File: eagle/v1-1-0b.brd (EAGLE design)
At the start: 313 x 132.9 mm, 176 parts, among them J1 CR22A-44D-2.54DSA(70), J3 26-60-4040, J4 AUDIO_JACK_3.5MM_PTH, J5 DIN5, SW1 3PDT-AQ-SWITCH, SW2 9077-1, U10 7805, U11 74LS10N, U13 74LS04N, U14 4528N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

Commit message: 8/19/2020 updates
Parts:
- removed JP4: (no value), aquarius2:1X01
- added JP1: (no value), aquarius2:1X01
- moved JP2 5.93 mm to (144.5, 48.1)
- moved JP3 4.06 mm to (148.6, 48.0)
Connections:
- net N$122: now also JP1.1; no longer JP2.1
- net N$19: now also JP2.1; no longer JP3.1
- net PALSW: now also JP3.1; no longer JP4.1
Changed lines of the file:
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@@
 <layer number="47" name="Measures" color="7" fill="1" visible="yes" active="yes"/>
 <layer number="48" name="Document" color="7" fill="1" visible="no" active="yes"/>
-<layer number="49" name="Reference" color="7" fill="1" visible="no" active="yes"/>
+<layer number="49" name="Reference" color="7" fill="1" visible="yes" active="yes"/>
 <layer number="50" name="dxf" color="7" fill="1" visible="yes" active="yes"/>
 <layer number="51" name="tDocu" color="7" fill="1" visible="yes" active="yes"/>
@@
 <wire x1="44.45" y1="9.906" x2="45.974" y2="11.6078" width="0.0762" layer="21"/>
 <wire x1="45.974" y1="11.6078" x2="45.974" y2="11.176" width="0.0762" layer="21"/>
+<frame x1="-11.176" y1="-13.462" x2="333.248" y2="144.78" columns="5" rows="3" layer="49"/>
 </plain>
 <attributes>
@@
 <attribute name="NAME" x="144.2974" y="30.3784" size="1.27" layer="21"/>
 </element>
-<element name="JP2" library="aquarius2" package="1X01" package3d_urn="urn:adsk.eagle:package:22485/2" value="" x="148.5392" y="43.7134" smashed="yes">
+<element name="JP1" library="aquarius2" package="1X01" package3d_urn="urn:adsk.eagle:package:22485/2" value="" x="148.5392" y="43.7134" smashed="yes">
 <attribute name="POPULARITY" value="64" x="148.5392" y="43.7134" size="1.778" layer="27" display="off"/>
 <attribute name="VALUE" x="147.2692" y="40.5384" size="1.27" layer="27"/>
 </element>
-<element name="JP3" library="aquarius2" package="1X01" package3d_urn="urn:adsk.eagle:package:22485/2" value="" x="144.5006" y="48.0568" smashed="yes">
+<element name="JP2" library="aquarius2" package="1X01" package3d_urn="urn:adsk.eagle:package:22485/2" value="" x="144.5006" y="48.0568" smashed="yes">
 <attribute name="POPULARITY" value="64" x="144.5006" y="48.0568" size="1.778" layer="27" display="off"/>
 <attribute name="VALUE" x="143.2306" y="44.8818" size="1.27" layer="27"/>
 </element>
-<element name="JP4" library="aquarius2" package="1X01" package3d_urn="urn:adsk.eagle:package:22485/2" value="" x="148.5646" y="48.0314" smashed="yes">
+<element name="JP3" library="aquarius2" package="1X01" package3d_urn="urn:adsk.eagle:package:22485/2" value="" x="148.5646" y="48.0314" smashed="yes">
 <attribute name="POPULARITY" value="64" x="148.5646" y="48.0314" size="1.778" layer="27" display="off"/>
 <attribute name="VALUE" x="147.2946" y="44.8564" size="1.27" layer="27"/>
@@
 </element>
 <element name="C22" library="aq-rcl" package="C050-025X085" value=".1uF" x="46.6852" y="45.9486" smashed="yes" rot="R270">
-<attribute name="NAME" x="46.6852" y="50.5206" size="0.8128" layer="25" ratio="10" align="bottom-center"/>
+<attribute name="NAME" x="46.6852" y="50.5206" size="0.6096" layer="25" ratio="10" align="bottom-center"/>
+<attribute name="VALUE" x="46.6852" y="41.3766" size="0.6096" layer="27" ratio="10" align="top-center"/>
 </element>
 <element name="C26" library="aq-rcl" package="C050-025X085" value=".1uF" x="11.8618" y="45.7962" smashed="yes" rot="R270">
@@
 </element>
 <element name="C20" library="aq-rcl" package="C050-025X090" value=".1uF" x="84.4296" y="45.2882" smashed="yes" rot="R270">
-<attribute name="NAME" x="84.4296" y="50.2412" size="0.8128" layer="25" ratio="10" align="bottom-center"/>
+<attribute name="NAME" x="84.4296" y="50.2412" size="0.6096" layer="25" ratio="10" align="bottom-center"/>
+<attribute name="VALUE" x="84.4296" y="40.4622" size="0.6096" layer="27" ratio="10" align="top-center"/>
 </element>
 <element name="C30" library="aq-rcl" package="E2,5-6" package3d_urn="urn:adsk.eagle:package:23349/1" value="10uF @ 16v" x="142.4686" y="60.579" smashed="yes" rot="R270">
@@
 </element>
 <element name="C36" library="aq-rcl" package="C050-024X044" package3d_urn="urn:adsk.eagle:package:23643/1" value=".01uF" x="137.9728" y="92.4306" smashed="yes">
-<attribute name="NAME" x="135.8138" y="93.8276" size="0.8128" layer="25" ratio="10"/>
+<attribute name="NAME" x="135.5598" y="93.8276" size="0.8128" layer="25" ratio="10"/>
 <attribute name="POPULARITY" value="14" x="137.9728" y="92.4306" size="1.778" layer="27" display="off"/>
 <attribute name="SPICEPREFIX" value="C" x="137.9728" y="92.4306" size="1.778" layer="27" display="off"/>
+<attribute name="VALUE" x="138.3538" y="93.8276" size="0.8128" layer="27" ratio="10"/>
 </element>
 <element name="C17" library="aq-rcl" package="C050-025X090" value=".1uF" x="81.661" y="68.453" smashed="yes" rot="R270">
@@
 <attribute name="POPULARITY" value="14" x="195.1736" y="81.2038" size="1.778" layer="27" display="off"/>
 <attribute name="SPICEPREFIX" value="C" x="195.1736" y="81.2038" size="1.778" layer="27" display="off"/>
+<attribute name="VALUE" x="195.7578" y="82.6262" size="0.8128" layer="27" ratio="10"/>
 </element>
 <element name="XTAL1" library="special" library_urn="urn:adsk.eagle:library:367" package="Q" package3d_urn="urn:adsk.eagle:package:26649/1" value="" x="177.673" y="88.9" smashed="yes" rot="R180">
@@
 <wire x1="115.70919375" y1="50.1904" x2="115.70919375" y2="46.67300625" width="0.508" layer="1"/>
 <wire x1="117.1194" y1="45.2628" x2="115.70919375" y2="46.67300625" width="0.508" layer="1"/>
-<contactref element="JP2" pad="1"/>
+<contactref element="JP1" pad="1"/>
 <wire x1="148.5392" y1="43.7134" x2="148.4884" y2="43.6626" width="0.508" layer="1"/>
 <wire x1="148.4884" y1="43.6626" x2="146.431" y2="43.6626" width="0.508" layer="1"/>
@@
 <wire x1="180.848" y1="81.026" x2="184.5564" y2="77.3176" width="0.508" layer="1"/>
 <wire x1="184.5564" y1="77.3176" x2="184.5564" y2="71.9582" width="0.508" layer="1"/>
-<contactref element="JP4" pad="1"/>
+<contactref element="JP3" pad="1"/>
 <wire x1="148.5646" y1="48.0314" x2="148.5392" y2="48.0568" width="0.508" layer="16"/>
 <wire x1="148.5392" y1="48.0568" x2="148.5392" y2="50.3936" width="0.508" layer="16"/>
@@
 <wire x1="140.4874" y1="50.1904" x2="140.4874" y2="49.0728" width="0.508" layer="1"/>
 <wire x1="141.9352" y1="47.625" x2="140.4874" y2="49.0728" width="0.508" layer="1"/>
-<contactref element="JP3" pad="1"/>
+<contactref element="JP2" pad="1"/>
 <wire x1="144.5006" y1="48.0568" x2="144.0688" y2="47.625" width="0.508" layer="1"/>
 <wire x1="144.0688" y1="47.625" x2="141.9352" y2="47.625" width="0.508" layer="1"/>

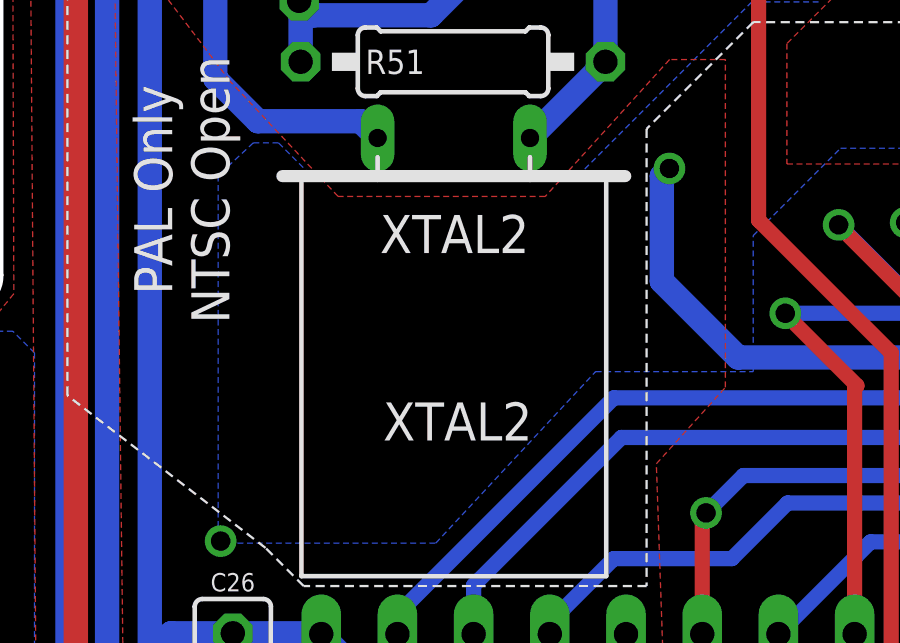
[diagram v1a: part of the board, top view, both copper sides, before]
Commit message: Edits for component values
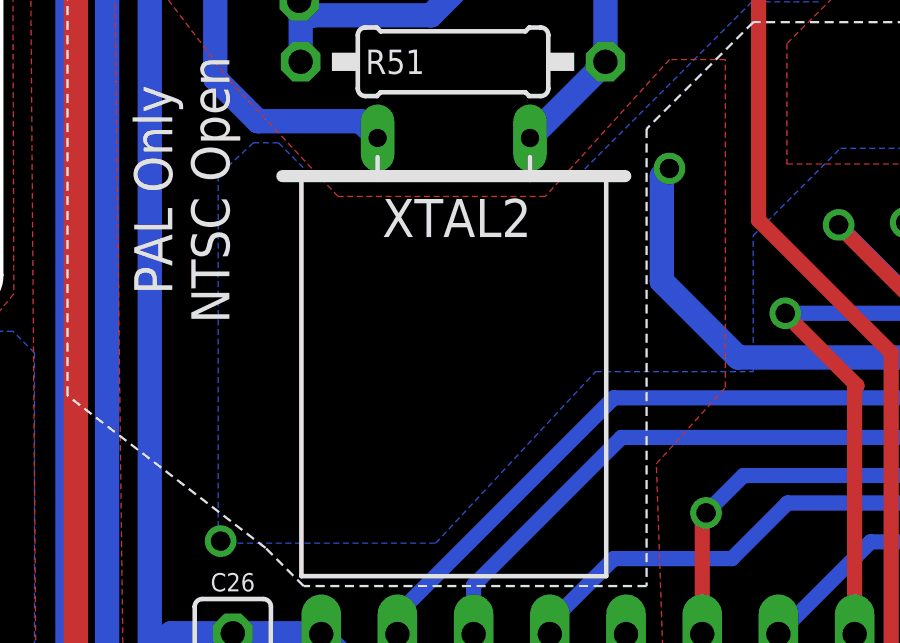
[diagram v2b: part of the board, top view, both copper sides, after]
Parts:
- XTAL1: value (none) -> 7.15909 MhZ
- XTAL2: value (none) -> 7.15909 Mhz
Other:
- board text added: "PAL 8.867238 Mhz"
- board text removed: "XTAL2"
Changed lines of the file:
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@@
 <text x="241.808" y="35.306" size="1.778" layer="21" align="center">Z80 CPU</text>
 <text x="108.966" y="114.3" size="1.778" layer="21" align="center">RF Modulator</text>
-<text x="19.2532" y="62.2808" size="1.27" layer="21" rot="R180" align="center">XTAL2</text>
 <text x="266.7" y="54.102" size="1.778" layer="21" align="center">Aquarius Motherboard v1.1.0
 Rev B - 17 AUG 2020
@@
 <wire x1="45.974" y1="11.6078" x2="45.974" y2="11.176" width="0.0762" layer="21"/>
 <frame x1="-11.176" y1="-13.462" x2="333.248" y2="144.78" columns="5" rows="3" layer="49"/>
+<text x="184.2262" y="87.6554" size="0.8128" layer="27">PAL 8.867238 Mhz</text>
+<text x="184.277" y="88.9762" size="0.762" layer="27">NTSC</text>
 </plain>
 <attributes>
@@
 <attribute name="OC_NEWARK" value="unknown" x="197.8914" y="21.9964" size="1.778" layer="27" display="off"/>
 <attribute name="POPULARITY" value="1" x="197.8914" y="21.9964" size="1.778" layer="27" display="off"/>
-<attribute name="VALUE" x="191.5414" y="18.8214" size="1.27" layer="27" ratio="10"/>
+<attribute name="VALUE" x="196.0372" y="23.9014" size="1.27" layer="27" ratio="10"/>
 </element>
 <element name="U9" library="74xx-us" library_urn="urn:adsk.eagle:library:88" package="DIL16" package3d_urn="urn:adsk.eagle:package:922/2" value="74367N" x="204.1906" y="13.7414" smashed="yes">
@@
 <attribute name="VALUE" x="195.7578" y="82.6262" size="0.8128" layer="27" ratio="10"/>
 </element>
-<element name="XTAL1" library="special" library_urn="urn:adsk.eagle:library:367" package="Q" package3d_urn="urn:adsk.eagle:package:26649/1" value="" x="177.673" y="88.9" smashed="yes" rot="R180">
+<element name="XTAL1" library="special" library_urn="urn:adsk.eagle:library:367" package="Q" package3d_urn="urn:adsk.eagle:package:26649/1" value="7.15909 MhZ" x="177.673" y="88.9" smashed="yes" rot="R180">
 <attribute name="NAME" x="180.2892" y="87.7062" size="1.27" layer="25" ratio="10" rot="R180"/>
 <attribute name="POPULARITY" value="12" x="177.673" y="88.9" size="1.778" layer="27" rot="R180" display="off"/>
-<attribute name="VALUE" x="180.9242" y="90.2462" size="1.27" layer="27" ratio="10" rot="R180"/>
+<attribute name="VALUE" x="187.7822" y="88.9508" size="0.8128" layer="27" ratio="10"/>
 </element>
 <element name="CT1" library="aq-rcl" package="CTRIM808-BC" package3d_urn="urn:adsk.eagle:package:23766/1" value="" x="191.897" y="96.4438" smashed="yes" rot="MR180">
@@
 <attribute name="VALUE" x="22.1488" y="68.0212" size="0.8128" layer="27" ratio="10" align="center-right"/>
 </element>
-<element name="XTAL2" library="special" library_urn="urn:adsk.eagle:library:367" package="Q" package3d_urn="urn:adsk.eagle:package:26649/1" value="" x="19.2278" y="57.8612" smashed="yes" rot="R180">
-<attribute name="NAME" x="21.844" y="56.6674" size="1.27" layer="25" ratio="10" rot="R180"/>
+<element name="XTAL2" library="special" library_urn="urn:adsk.eagle:library:367" package="Q" package3d_urn="urn:adsk.eagle:package:26649/1" value="7.15909 Mhz" x="19.2278" y="57.8612" smashed="yes" rot="R180">
+<attribute name="NAME" x="19.3294" y="62.8142" size="1.27" layer="25" ratio="10" rot="R180" align="center"/>
 <attribute name="POPULARITY" value="12" x="19.2278" y="57.8612" size="1.778" layer="27" rot="R180" display="off"/>
-<attribute name="VALUE" x="22.479" y="59.2074" size="1.27" layer="27" ratio="10" rot="R180"/>
+<attribute name="VALUE" x="19.431" y="61.4426" size="0.8128" layer="27" ratio="10" align="center"/>
 </element>
 <element name="R52" library="aq-rcl" package="0207/10" package3d_urn="urn:adsk.eagle:package:23491/2" value="56k" x="85.1154" y="27.9146" smashed="yes" rot="R90">
